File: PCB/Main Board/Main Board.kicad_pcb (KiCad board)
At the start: 2 copper layers, 152.4 x 134.6 mm, 257 parts, among them J101 Conn_Coaxial, J102 Conn_Coaxial, J103 Conn_Coaxial, J104 Conn_Coaxial, J105 Conn_01x01_Pin, J201 USB_C_Receptacle_USB2.0_16P, J801 Conn_01x03_Pin, J802 Screw_Terminal_01x03, K301 AGQ200A12, K401 AGQ200A12, K501 AGQ200A12, K502 AGQ200A12, K503 AGQ200A12, K504 AGQ200A12, K505 AGQ200A12, Q301 TIP41C, Q302 TIP42C, Q401 TIP41C, Q402 TIP42C, Q403 TIP41C, Q404 TIP42C, SW201 SW_Push, SW202 SW_Push, U201 USBLC6-2SC6, U202 STM32F446RETx, U203 ULN2003, U301 DG201, U302 OPA2197xD, U303 OPA2376xxD, U304 OPA2197xD, U401 OPA2197xD, U402 DG201, U403 OPA2197xD, U404 OPA2197xD, U601 INA828D, U602 DG201, U603 OPA2197xD, U604 DG201, U605 OPA2376xxD, U701 INA828D, U702 DG201, U703 OPA2376xxD, U801 LM317_SOT-223, U802 LM317_SOT-223, U803 LM317_SOT-223, U804 LM337_SOT223, Y201 8MHz

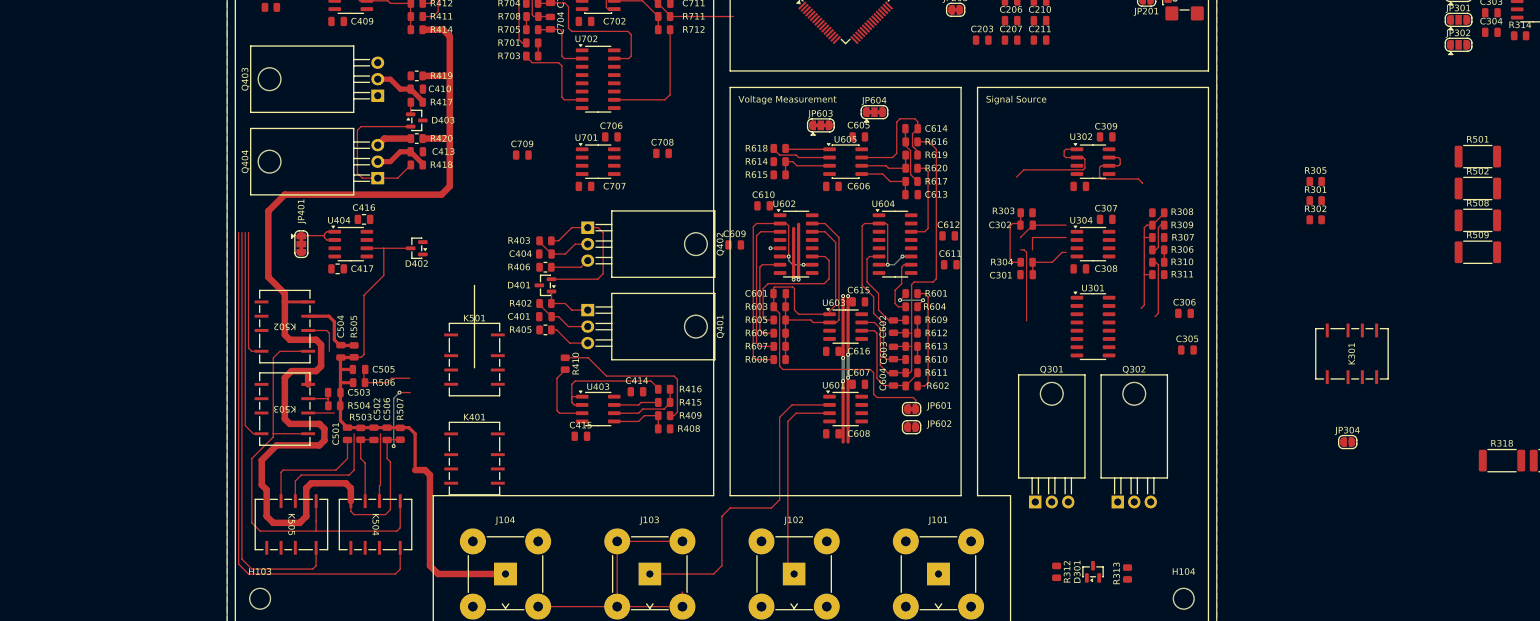
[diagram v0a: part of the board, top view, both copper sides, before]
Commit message: move resistors
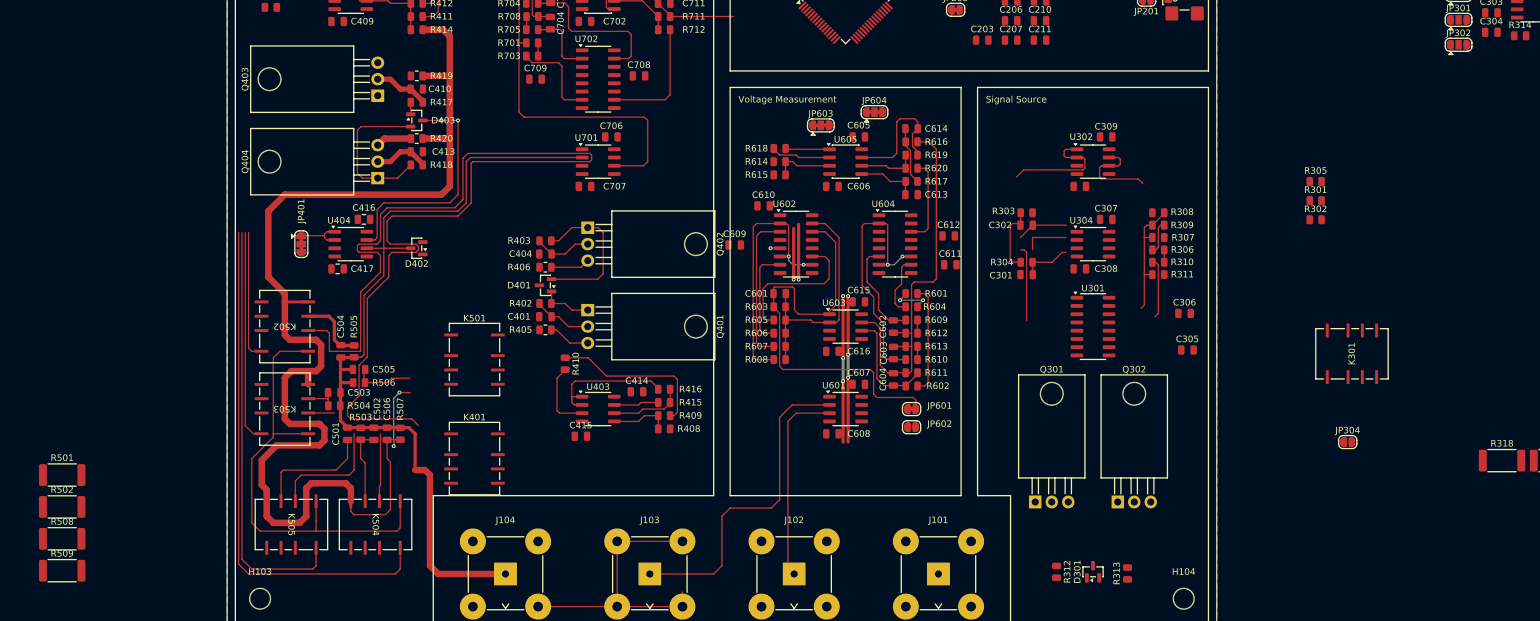
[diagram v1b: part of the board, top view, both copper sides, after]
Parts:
- moved R501 223.5 mm to (19.1, 137.2)
- moved R502 223.5 mm to (19.1, 142.1)
- moved R508 223.5 mm to (19.1, 147.0)
- moved R509 223.5 mm to (19.1, 151.9)
- moved C708 12.5 mm to (107.9, 75.7)
- moved C709 11.9 mm to (91.9, 76.2)
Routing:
- net GUARD: track 350.0 -> 436.5 mm
- net Net-(R701-Pad1): track 11.8 -> 54.9 mm
- net /Auto-Balancing Bridge/In: track 88.7 -> 131.5 mm
- net Net-(D403-K-Pad3): track 0.00 -> 36.3 mm, vias 0 -> 2

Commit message: sig source layout prelim
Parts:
- moved RN301 86.7 mm to (169.7, 96.4)
- moved R319 75.8 mm to (177.8, 130.3), turned to 180 degrees
- moved R314 74.8 mm to (171.7, 90.1), turned to 180 degrees
- moved U303 70.7 mm to (177.4, 83.6)
- moved R316 69.3 mm to (185.7, 130.3), turned to 180 degrees
- moved JP301 69.0 mm to (166.8, 82.3), turned to 180 degrees
- moved JP302 68.8 mm to (166.8, 85.2), turned to 180 degrees
- moved C304 66.4 mm to (175.4, 87.4)
- moved R315 63.0 mm to (185.6, 134.4)
- moved R318 63.0 mm to (177.8, 134.4), turned to 180 degrees
- moved C303 61.3 mm to (179.5, 79.8)
- moved C315 55.4 mm to (187.2, 82.3)
- moved JP304 55.0 mm to (162.3, 137.5)
- moved K301 53.6 mm to (165.4, 130.4), turned to 0 degrees
- moved JP303 51.4 mm to (187.4, 84.7), turned to 180 degrees
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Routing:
- net +1.65VA: track 6.83 -> 64.1 mm, vias 0 -> 4
- net (no net): track 55.9 -> 0.00 mm
- net Net-(JP303-C): track 0.00 -> 31.7 mm
- net Net-(R302-Pad2): track 0.00 -> 25.1 mm
- net Net-(R310-Pad2): track 9.28 -> 27.2 mm
- net Net-(U303B-+): track 0.00 -> 17.7 mm
- net Net-(U304B--): track 19.2 -> 36.7 mm, vias 0 -> 2
- net Net-(JP301-C): track 0.00 -> 16.2 mm
- net Net-(U302A--): track 0.00 -> 15.4 mm
- net Net-(R301-Pad1): track 0.00 -> 14.2 mm, vias 0 -> 2
- net +18V: track 49.2 -> 62.4 mm
- net Net-(JP302-C): track 0.00 -> 13.2 mm, vias 0 -> 2
- net -18V: track 48.6 -> 61.5 mm
- net Net-(C302-Pad2): track 13.1 -> 25.6 mm, vias 0 -> 4
- net Net-(U304A--): track 0.00 -> 12.4 mm
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
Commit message: yipppeee
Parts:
- added REF**: R_0805_2012Metric, Resistor_SMD:R_0805_2012Metric, F.Cu at (69.7, 136.0)
- added REF**: R_0805_2012Metric, Resistor_SMD:R_0805_2012Metric, F.Cu at (71.8, 136.0)
- added REF**: R_0805_2012Metric, Resistor_SMD:R_0805_2012Metric, F.Cu at (69.7, 139.6)
- added REF**: R_0805_2012Metric, Resistor_SMD:R_0805_2012Metric, F.Cu at (71.8, 139.6)
- moved R502 43.2 mm to (62.2, 139.7), turned to 180 degrees
- moved R501 43.2 mm to (62.2, 135.9), turned to 180 degrees
- moved R503 43.1 mm to (23.5, 142.2)
- moved R509 37.6 mm to (54.6, 139.7), turned to 180 degrees
- moved R508 37.2 mm to (54.6, 135.9), turned to 180 degrees
- moved C406 24.2 mm to (71.6, 50.0)
- moved K401 21.3 mm to (76.2, 114.3)
- moved C506 10.7 mm to (77.7, 137.2), turned to 0 degrees
- moved K501 9.92 mm to (76.2, 127.0)
- moved R507 7.89 mm to (77.7, 135.1), turned to 0 degrees
- moved C502 5.25 mm to (67.7, 136.0)
- moved C505 5.21 mm to (68.6, 124.5)
- moved R506 5.21 mm to (68.6, 126.5)
- moved C407 4.33 mm to (54.6, 50.8)
- moved C414 4.10 mm to (103.6, 123.2)
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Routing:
- net /Auto-Balancing Bridge/DC_INT_ISO: track 0.00 -> 203.4 mm, vias 0 -> 2
- net /Auto-Balancing Bridge/R_SEL_100k: track 0.00 -> 187.1 mm
- net GUARD: track 436.5 -> 585.9 mm
- net +12V: track 70.2 -> 190.1 mm, vias 0 -> 8
- net /Auto-Balancing Bridge/R_SEL_1k: track 32.7 -> 102.3 mm
- net /Auto-Balancing Bridge/R_SEL_10: track 65.3 -> 133.3 mm
- net /Auto-Balancing Bridge/R_SEL_10k: track 20.0 -> 87.9 mm
- net /Auto-Balancing Bridge/R_SEL_100: track 80.2 -> 144.1 mm
- net /Auto-Balancing Bridge/In: track 131.5 -> 176.5 mm
- net +1.65VA: track 64.1 -> 33.5 mm, vias 4 -> 0
- net Net-(R404-Pad2): track 25.1 -> 51.7 mm
- net Net-(U403A-+): track 10.9 -> 28.9 mm
- net Net-(JP301-C): track 16.2 -> 0.00 mm
- net Net-(U304A--): track 12.4 -> 0.00 mm
- net Net-(D301-K-Pad3): track 6.82 -> 0.00 mm
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
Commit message: yup
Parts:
- removed REF** (x4): R_0805_2012Metric, Resistor_SMD:R_0805_2012Metric
- removed U203: ULN2003, Package_SO:SOIC-16_3.9x9.9mm_P1.27mm
- added U402: ULN2003, Package_SO:SOIC-16_3.9x9.9mm_P1.27mm, F.Cu at (63.5, 38.1)
- moved C808 39.4 mm to (113.3, 46.4)
- moved C812 39.4 mm to (113.6, 35.0)
- moved R804 39.4 mm to (105.2, 40.7)
- moved R808 39.4 mm to (109.6, 35.0)
- moved U804 39.4 mm to (111.8, 40.6)
- moved C811 33.0 mm to (169.5, 35.0)
- moved R803 33.0 mm to (161.1, 40.7)
- moved C807 33.0 mm to (169.3, 46.3)
- moved D804 33.0 mm to (172.6, 33.9)
- moved FB801 33.0 mm to (169.6, 30.6)
- moved R807 33.0 mm to (165.6, 35.0)
- moved R809 33.0 mm to (169.5, 32.8)
- moved U803 33.0 mm to (167.6, 40.6)
- moved C805 31.8 mm to (131.2, 46.3)
- moved C809 31.8 mm to (131.4, 35.0)
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- renumbered C404 to C402, C405 to C403, C406 to C404, C407 to C405, C408 to C406, C409 to C407, C410 to C408, C413 to C409, C414 to C410, C415 to C411, C416 to C412, C417 to C413, U402 to U403, U403 to U404, U404 to U405
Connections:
- K401 pad 8: /Auto-Balancing Bridge/DC_INT_ISO -> /Auto-Balancing Bridge/DC_ISO
- K501 pad 8: /Auto-Balancing Bridge/R_SEL_100k -> /Auto-Balancing Bridge/SEL_100k
- K502 pad 8: /Auto-Balancing Bridge/R_SEL_10k -> /Auto-Balancing Bridge/SEL_10k
- K503 pad 8: /Auto-Balancing Bridge/R_SEL_1k -> /Auto-Balancing Bridge/SEL_1k
- K504 pad 8: /Auto-Balancing Bridge/R_SEL_100 -> /Auto-Balancing Bridge/SEL_100
- K505 pad 8: /Auto-Balancing Bridge/R_SEL_10 -> /Auto-Balancing Bridge/SEL_10
- U202 pad 29: Net-(U202-PB10) -> /Auto-Balancing Bridge/R_SEL_10k
- U202 pad 33: Net-(U202-PB12) -> /Auto-Balancing Bridge/R_SEL_100
- U202 pad 34: Net-(U202-PB13) -> /Auto-Balancing Bridge/R_SEL_10
- U202 pad 35: Net-(U202-PB14) -> /Auto-Balancing Bridge/DC_INT_ISO
- U202 pad 36: Net-(U202-PB15) -> /Processor/SIG_SOURCE
- U202 pad 61: Net-(U202-PB8) -> /Auto-Balancing Bridge/R_SEL_100k
- U202 pad 62: Net-(U202-PB9) -> /Auto-Balancing Bridge/R_SEL_1k
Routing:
- net /Auto-Balancing Bridge/DC_ISO: track 0.00 -> 205.6 mm, vias 0 -> 2
- net /Auto-Balancing Bridge/DC_INT_ISO: track 203.4 -> 0.00 mm, vias 2 -> 0
- net /Auto-Balancing Bridge/SEL_100k: track 0.00 -> 189.4 mm
- net /Auto-Balancing Bridge/R_SEL_100k: track 187.1 -> 0.00 mm
- net /Auto-Balancing Bridge/SEL_100: track 0.00 -> 146.3 mm
- net /Auto-Balancing Bridge/R_SEL_100: track 144.1 -> 0.00 mm
- net /Auto-Balancing Bridge/SEL_10: track 0.00 -> 135.5 mm
- net /Auto-Balancing Bridge/R_SEL_10: track 133.3 -> 0.00 mm
- net /Auto-Balancing Bridge/SEL_1k: track 0.00 -> 104.5 mm
- net /Auto-Balancing Bridge/R_SEL_1k: track 102.3 -> 0.00 mm
- net /Auto-Balancing Bridge/SEL_10k: track 0.00 -> 90.2 mm
- net /Auto-Balancing Bridge/R_SEL_10k: track 87.9 -> 0.00 mm
- net -18V: track 65.8 -> 130.7 mm, vias 4 -> 6
- net +18V: track 63.9 -> 125.3 mm, vias 4 -> 6
- net Net-(D403-A): track 24.4 -> 18.1 mm
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
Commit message: sig source finished
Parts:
- removed the C311 at (202.1, 147.2)
- removed the C312 at (202.0, 143.9)
- removed the C313 at (210.5, 142.4)
- removed the C314 at (210.3, 148.0)
- removed the C408 at (73.7, 77.7)
- removed the C409 at (73.7, 87.4)
- removed the R312 at (191.7, 138.7)
- removed the R317 at (181.8, 127.2)
- removed the R405 at (91.4, 114.8)
- removed the R406 at (91.4, 105.2)
- removed R419, R420: 100m, Resistor_SMD:R_0805_2012Metric
- added C301: 10µ, Capacitor_SMD:C_0805_2012Metric, F.Cu at (184.5, 129.8)
- added C303: 1u, Capacitor_SMD:C_0805_2012Metric, F.Cu at (179.5, 124.3)
- added C305: 10µ, Capacitor_SMD:C_0805_2012Metric, F.Cu at (170.0, 129.8)
- added C403: 1u, Capacitor_SMD:C_0805_2012Metric, F.Cu at (38.7, 103.3)
- added C404: 1u, Capacitor_SMD:C_0805_2012Metric, F.Cu at (38.7, 106.3)
- added C405: 10µ, Capacitor_SMD:C_0805_2012Metric, F.Cu at (38.7, 109.3)
- added C406: 10µ, Capacitor_SMD:C_0805_2012Metric, F.Cu at (38.7, 112.3)
- added Q303: 2N7002, Package_TO_SOT_SMD:SOT-23, F.Cu at (183.9, 156.8)
- added R309: 2k, Resistor_SMD:R_0805_2012Metric, F.Cu at (173.8, 129.8)
- added R314: 100, Resistor_SMD:R_0805_2012Metric, F.Cu at (171.9, 145.7)
- added R315: 100, Resistor_SMD:R_0805_2012Metric, F.Cu at (169.8, 142.2)
- added R316: 100, Resistor_SMD:R_0805_2012Metric, F.Cu at (169.8, 145.7)
- added R320: 2k, Resistor_SMD:R_0805_2012Metric, F.Cu at (180.9, 129.8)
- Q301, Q302, Q401, Q404: moved to B.Cu
- Q402: renamed from Q403; moved to B.Cu
- Q403: renamed from Q402; moved to B.Cu
- R313: value 2k -> 100
- moved J101 208.2 mm to (166.5, 157.1), turned to -90 degrees
- moved C306 79.5 mm to (163.6, 158.2), turned to -90 degrees
- moved C401 55.0 mm to (38.7, 97.2)
- moved C402 52.8 mm to (38.7, 100.2)
- moved Q401 46.4 mm to (67.4, 78.8), turned to 90 degrees
- moved Q402 46.1 mm to (99.8, 111.8), turned to -90 degrees
- moved Q403 33.5 mm to (67.4, 91.5), turned to 90 degrees
- moved Q404 33.0 mm to (99.8, 99.1), turned to -90 degrees
- moved K301 26.6 mm to (176.2, 154.7), turned to -90 degrees
- moved D301 21.1 mm to (177.3, 128.8), turned to 90 degrees
- moved R313 20.9 mm to (171.9, 142.2), turned to -90 degrees
- moved R307 17.3 mm to (175.0, 144.0), turned to -90 degrees
- moved JP301 15.6 mm to (169.2, 151.4), turned to 90 degrees
- moved R308 14.7 mm to (183.2, 144.0), turned to -90 degrees
- moved R305 13.5 mm to (187.3, 144.0), turned to -90 degrees
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- renumbered C209 to C201, C204 to C202, C201 to C203, C202 to C204, C203 to C205, C205 to C206, C206 to C207, C207 to C208, C208 to C209, C301 to C304, C315 to C306, C303 to C307, C305 to C308, C307 to C309, C309 to C310, C304 to C311, C306 to C312, C308 to C313, C310 to C314, C403 to C407, C404 to C408, C406 to C409, C412 to C411, C405 to C412, C407 to C413, C411 to C414, C413 to C415, C602 to C601, C614 to C602, C613 to C604, C604 to C605, C605 to C606, C609 to C608, C611 to C609, C615 to C610, C606 to C611, C608 to C612, C610 to C613, C612 to C614, C616 to C615, C601 to C616, C703 to C701, C711 to C702, C704 to C703, C710 to C704, C701 to C706, C706 to C707, C702 to C709, C707 to C710, C709 to C711, C805 to C801, C809 to C802, C806 to C803, C810 to C804, C801 to C805, C803 to C806, C802 to C807, C804 to C808, C807 to C809, C811 to C810, C808 to C811, D403 to D402, D402 to D403, D803 to D801, D801 to D802, D802 to D803, J105 to J101, J101 to J102, J102 to J103, J103 to J104, J104 to J105, J802 to J801, J801 to J802, JP203 to JP202, JP202 to JP203, JP304 to JP301, JP303 to JP302, JP301 to JP303, JP302 to JP304, JP603 to JP601, JP604 to JP602, JP601 to JP603, JP602 to JP604, K505 to K501, K504 to K502, K502 to K504, K501 to K505, R205 to R204, R206 to R205, R207 to R206, R208 to R207, R204 to R208, R307 to R301, R311 to R302, R308 to R303, R315 to R304, R318 to R305, R309 to R306, R316 to R307, R319 to R308, R306 to R310, R310 to R311, R304 to R312, R303 to R317, R305 to R318, R301 to R319, R302 to R321, R314 to R322, R404 to R401, R408 to R402, R415 to R403, R409 to R404, R416 to R405, R402 to R406, R417 to R407, R410 to R408, R401 to R409, R403 to R410, R418 to R412, R407 to R413, R412 to R414, R413 to R415, R414 to R416, R508 to R502, R502 to R503, R509 to R504, R503 to R505, R504 to R506, R505 to R507, R506 to R508, R507 to R509, R609 to R601, R612 to R602, R601 to R603, R610 to R605, R613 to R606, R616 to R607, R617 to R608, R619 to R609, R602 to R610, R620 to R612, R618 to R613, R608 to R616, R603 to R617, R605 to R618, R606 to R619, R607 to R620, R704 to R701, R707 to R702, R701 to R703, R703 to R704, R708 to R706, R709 to R707, R710 to R708, R711 to R709, R702 to R710, R706 to R711, R805 to R801, R801 to R802, R806 to R803, R802 to R804, R807 to R805, R809 to R806, R803 to R807, R804 to R808, R808 to R809, SW202 to SW201, SW201 to SW202, U302 to U301, U301 to U302, U304 to U303, U303 to U304, U404 to U401, U401 to U402, U405 to U403, U403 to U404, U402 to U405, U604 to U601, U601 to U602, U605 to U603, U603 to U604, U602 to U605, U702 to U701, U701 to U702
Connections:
- C402 pad 2: -18V -> +18V
- D301 pad 3: Net-(D301-K-Pad3) -> Net-(C303-Pad2)
- D401 pad 3: Net-(D401-K-Pad3) -> Net-(C403-Pad2)
- D402 pad 3: Net-(D403-K-Pad3) -> Net-(C404-Pad2)
- K301 pad 8: /Processor/SIG_SOURCE -> /Signal Source/RELAY_DRIVE
- Q402 pad 3: Net-(Q403-E) -> /Auto-Balancing Bridge/OUT+
- Q403 pad 3: Net-(Q402-E) -> Net-(Q401-E)
- Q404 pad 3: Net-(Q404-E) -> /Auto-Balancing Bridge/OUT+
- R313 pad 1: Net-(D301-A) -> Net-(Q301-E)
- R313 pad 2: -18V -> Net-(R313-Pad2)
- R401 pad 2: Net-(R404-Pad2) -> Net-(Q401-E)
- R404 pad 2: Net-(R404-Pad2) -> Net-(Q401-E)
- R408 pad 1: Net-(R404-Pad2) -> Net-(Q401-E)
- U303 pad 7: Net-(D301-K-Pad3) -> Net-(C303-Pad1)
- U402 pad 1: Net-(D401-K-Pad3) -> Net-(C403-Pad1)
- U403 pad 7: Net-(D403-K-Pad3) -> Net-(C404-Pad1)
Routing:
- net /Signal Source/AUX_DAC_OUT: track 7.94 -> 112.0 mm
- net /Processor/SIG_SOURCE: track 0.00 -> 82.0 mm
- net Net-(Q401-E): track 8.48 -> 66.0 mm
- net Net-(R404-Pad2): track 51.7 -> 0.00 mm
- net Net-(D403-K-Pad3): track 34.7 -> 0.00 mm, vias 2 -> 0
- net (no net): track 0.00 -> 34.7 mm, vias 0 -> 2
- net +1.65VA: track 33.5 -> 58.4 mm, vias 0 -> 4
- net /Signal Source/Out: track 0.00 -> 22.6 mm
- net /Auto-Balancing Bridge/OUT+: track 211.5 -> 225.2 mm
- net Net-(Q301-E): track 5.67 -> 19.3 mm
- net Net-(K301-Pad2): track 0.00 -> 12.9 mm
- net Net-(R307-Pad2): track 0.00 -> 10.6 mm
- net Net-(R304-Pad2): track 0.00 -> 10.6 mm
- net Net-(U303B--): track 36.7 -> 26.5 mm
- net Net-(D301-A): track 0.00 -> 10.1 mm
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
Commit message: minor
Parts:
- J101: footprint Connector_PinHeader_2.54mm:PinHeader_1x01_P2.54mm_Vertical -> Connector_PinHeader_2.54mm:PinHeader_1x01_P2.54mm_Horizontal
- moved C306 1.91 mm to (165.6, 158.1)
- moved J101 1.91 mm to (168.4, 157.1)
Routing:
- net Net-(Q301-E): track 19.3 -> 41.8 mm, vias 0 -> 2
- net Net-(Q301-B): track 3.44 -> 19.3 mm
- net Net-(U303B--): track 26.5 -> 38.3 mm
- net +18V: track 125.3 -> 137.2 mm
- net -18V: track 133.7 -> 144.6 mm
- net Net-(U303A--): track 2.41 -> 13.0 mm
- net +1.65VA: track 58.4 -> 65.7 mm
- net Net-(D301-A): track 10.1 -> 12.5 mm
- net /Signal Source/AUX_DAC_OUT: track 112.0 -> 110.0 mm
- net Net-(JP302-C): track 31.7 -> 32.6 mm

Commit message: hello
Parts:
- added R501: 100, Resistor_SMD:R_0805_2012Metric, F.Cu at (71.9, 135.9)
- added R511: 100, Resistor_SMD:R_0805_2012Metric, F.Cu at (71.9, 139.4)
- added R512: 100, Resistor_SMD:R_0805_2012Metric, F.Cu at (69.8, 139.4)
- J105: renamed from J101; footprint Connector_PinHeader_2.54mm:PinHeader_1x01_P2.54mm_Horizontal -> Connector_PinHeader_2.54mm:PinHeader_1x01_P2.54mm_Vertical
- JP701, JP702: footprint Jumper:SolderJumper-3_P1.3mm_Bridged123_RoundedPad1.0x1.5mm -> Jumper:SolderJumper-3_P1.3mm_Bridged12_RoundedPad1.0x1.5mm
- Q302: renamed from Q301; footprint Package_TO_SOT_THT:TO-220-3_Horizontal_TabDown -> Package_TO_SOT_THT:TO-220-3_Horizontal_TabUp
- Q303: renamed from Q302; footprint Package_TO_SOT_THT:TO-220-3_Horizontal_TabDown -> Package_TO_SOT_THT:TO-220-3_Horizontal_TabUp
- Q401, Q404: footprint Package_TO_SOT_THT:TO-220-3_Horizontal_TabDown -> Package_TO_SOT_THT:TO-220-3_Horizontal_TabUp
- Q402: renamed from Q403; footprint Package_TO_SOT_THT:TO-220-3_Horizontal_TabDown -> Package_TO_SOT_THT:TO-220-3_Horizontal_TabUp
- Q403: renamed from Q402; footprint Package_TO_SOT_THT:TO-220-3_Horizontal_TabDown -> Package_TO_SOT_THT:TO-220-3_Horizontal_TabUp
- moved Y201 48.2 mm to (124.2, 69.3)
- moved R502 46.8 mm to (69.8, 135.9)
- moved Q403 45.4 mm to (68.6, 78.7), turned to 90 degrees
- moved Q401 44.0 mm to (96.5, 111.8), turned to -90 degrees
- moved JP702 38.8 mm to (99.6, 69.6)
- moved JP701 37.2 mm to (103.6, 57.4), turned to 180 degrees
- moved Q404 32.1 mm to (68.6, 91.5), turned to 90 degrees
- moved Q402 30.1 mm to (96.5, 99.1), turned to -90 degrees
- moved Q303 4.93 mm to (168.7, 136.9), turned to 0 degrees
- moved R404 4.15 mm to (53.3, 64.5), turned to 180 degrees
- moved R401 3.42 mm to (53.3, 62.5)
- moved C502 0.13 mm to (67.7, 135.9)
- turned Q302 to 0 degrees
- renumbered C203 to C201, C204 to C202, C205 to C203, C202 to C204, C206 to C205, C207 to C206, C208 to C207, C209 to C208, C201 to C209, C304 to C301, C307 to C303, C311 to C304, C308 to C305, C312 to C306, C309 to C307, C313 to C308, C310 to C309, C314 to C310, C303 to C311, C301 to C312, C305 to C313, C306 to C314, C403 to C401, C401 to C402, C405 to C403, C407 to C404, C408 to C405, C412 to C406, C409 to C407, C413 to C408, C404 to C409, C402 to C410, C406 to C411, C410 to C412, C414 to C413, C411 to C414, C616 to C601, C601 to C602, C605 to C604, C606 to C605, C611 to C606, C612 to C608, C608 to C609, C613 to C610, C609 to C611, C614 to C612, C604 to C613, C602 to C614, C610 to C615, C615 to C616, C706 to C701, C709 to C702, C701 to C703, C703 to C704, C707 to C706, C710 to C707, C711 to C709, C704 to C710, C702 to C711, C805 to C801, C807 to C802, C806 to C803, C808 to C804, C801 to C805, C803 to C806, C809 to C807, C811 to C808, C802 to C809, C804 to C810, C810 to C811, D403 to D402, D402 to D403, D802 to D801, D803 to D802, D801 to D803, J102 to J101, J103 to J102, J104 to J103, J105 to J104, J802 to J801, J801 to J802, JP203 to JP202, JP202 to JP203, JP303 to JP301, JP304 to JP302, JP302 to JP303, JP301 to JP304, JP603 to JP601, JP604 to JP602, JP601 to JP603, JP602 to JP604, K505 to K501, K504 to K502, K502 to K504, K501 to K505, Q303 to Q301, R208 to R204, R204 to R205, R205 to R206, R206 to R207, R207 to R208, R319 to R301, R321 to R302, R317 to R303, R312 to R304, R318 to R305, R310 to R306, R301 to R307, R303 to R308, R306 to R309, R311 to R310, R309 to R311, R320 to R312, R302 to R313, R322 to R314, R304 to R315, R307 to R316, R313 to R317, R315 to R318, R305 to R319, R308 to R320, R314 to R321, R316 to R322, R409 to R401, R406 to R402, R410 to R403, R401 to R404, R413 to R405, R402 to R406, R404 to R407, R411 to R409, R414 to R410, R415 to R411, R416 to R412, R403 to R413, R405 to R414, R407 to R415, R412 to R416, R505 to R502, R501 to R503, R503 to R504, R506 to R505, R507 to R506, R508 to R507, R509 to R508, R502 to R509, R504 to R510, R603 to R601, R610 to R602, R617 to R603, R618 to R605, R619 to R606, R620 to R607, R616 to R608, R601 to R609, R605 to R610, R602 to R612, R606 to R613, R607 to R616, R608 to R617, R613 to R618, R609 to R619, R612 to R620, R703 to R701, R710 to R702, R704 to R703, R701 to R704, R711 to R706, R702 to R707, R706 to R708, R707 to R709, R708 to R710, R709 to R711, R802 to R801, R804 to R802, R807 to R803, R808 to R804, R801 to R805, R803 to R806, R805 to R807, R809 to R808, R806 to R809, SW202 to SW201, SW201 to SW202, U302 to U301, U301 to U302, U304 to U303, U303 to U304, U402 to U401, U405 to U402, U404 to U403, U401 to U404, U403 to U405, U602 to U601, U605 to U602, U604 to U603, U601 to U604, U603 to U605, U702 to U701, U701 to U702
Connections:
- R502 pad 2: Net-(C502-Pad2) -> Net-(R502-Pad2)
- U202 pad 10: /Processor/VAmp.x3 -> unconnected-(U202-PC2-Pad10)
- U202 pad 11: /Processor/VAmp.~{x100} -> unconnected-(U202-PC3-Pad11)
- U202 pad 14: /Processor/VAmp.Out -> unconnected-(U202-PA0-Pad14)
- U202 pad 15: /Current Amplifier/Out -> unconnected-(U202-PA1-Pad15)
- U202 pad 16: /Processor/SW1 -> unconnected-(U202-PA2-Pad16)
- U202 pad 17: unconnected-(U202-PA3-Pad17) -> /Processor/VAmp.Out
- U202 pad 2: /Processor/IAmp.AC_100 -> unconnected-(U202-PC13-Pad2)
- U202 pad 24: /Processor/VAmp.AC_EN -> unconnected-(U202-PC4-Pad24)
- U202 pad 25: /Processor/VAmp.AC_100 -> unconnected-(U202-PC5-Pad25)
- U202 pad 29: /Auto-Balancing Bridge/R_SEL_10k -> unconnected-(U202-PB10-Pad29)
- U202 pad 3: /Processor/IAmp.AC_1k -> unconnected-(U202-PC14-Pad3)
- U202 pad 33: /Auto-Balancing Bridge/R_SEL_100 -> unconnected-(U202-PB12-Pad33)
- U202 pad 34: /Auto-Balancing Bridge/R_SEL_10 -> unconnected-(U202-PB13-Pad34)
- U202 pad 35: /Auto-Balancing Bridge/DC_INT_ISO -> unconnected-(U202-PB14-Pad35)
- U202 pad 36: /Processor/SIG_SOURCE -> unconnected-(U202-PB15-Pad36)
- U202 pad 37: /Processor/VAmp.AC_1k -> unconnected-(U202-PC6-Pad37)
- U202 pad 38: /Processor/VAmp.AC_10k -> unconnected-(U202-PC7-Pad38)
- U202 pad 39: /Current Amplifier//4 -> unconnected-(U202-PC8-Pad39)
- U202 pad 4: /Processor/IAmp.AC_10k -> unconnected-(U202-PC15-Pad4)
- U202 pad 40: /Current Amplifier/x1 -> unconnected-(U202-PC9-Pad40)
- U202 pad 51: /Current Amplifier/x3 -> unconnected-(U202-PC10-Pad51)
- U202 pad 52: /Current Amplifier/~{x100} -> unconnected-(U202-PC11-Pad52)
- U202 pad 53: /Processor/IAmp.AC_EN -> unconnected-(U202-PC12-Pad53)
- U202 pad 56: /Processor/Source.~{x4} -> /Auto-Balancing Bridge/DC_INT_ISO
- U202 pad 57: /Processor/Source./10 -> /Auto-Balancing Bridge/R_SEL_100k
- U202 pad 58: unconnected-(U202-PB6-Pad58) -> /Auto-Balancing Bridge/R_SEL_10k
- U202 pad 59: unconnected-(U202-PB7-Pad59) -> /Auto-Balancing Bridge/R_SEL_1k
- U202 pad 61: /Auto-Balancing Bridge/R_SEL_100k -> /Auto-Balancing Bridge/R_SEL_100
- U202 pad 62: /Auto-Balancing Bridge/R_SEL_1k -> /Auto-Balancing Bridge/R_SEL_10
- U202 pad 8: /Processor/VAmp./4 -> unconnected-(U202-PC0-Pad8)
- U202 pad 9: /Processor/VAmp.x1 -> /Current Amplifier/Out
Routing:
- net /Auto-Balancing Bridge/DC_INT_ISO: track 0.00 -> 85.4 mm
- net /Auto-Balancing Bridge/R_SEL_100k: track 0.00 -> 84.5 mm
- net /Auto-Balancing Bridge/R_SEL_10k: track 0.00 -> 83.8 mm
- net /Auto-Balancing Bridge/R_SEL_1k: track 0.00 -> 83.1 mm
- net /Auto-Balancing Bridge/R_SEL_100: track 0.00 -> 82.1 mm
- net /Auto-Balancing Bridge/R_SEL_10: track 0.00 -> 81.1 mm
- net -18V: track 144.6 -> 203.9 mm, vias 6 -> 10
- net +18V: track 137.2 -> 189.4 mm, vias 6 -> 10
- net Net-(Q302-E): track 41.8 -> 0.00 mm, vias 2 -> 0
- net Net-(D301-A): track 12.5 -> 54.3 mm, vias 0 -> 2
- net /Current Amplifier/Out: track 20.0 -> 42.1 mm
- net unconnected-(U202-PC0-Pad8): track 0.00 -> 19.3 mm
- net /Processor/VAmp.Out: track 19.9 -> 36.8 mm
- net Net-(Q401-E): track 66.0 -> 51.7 mm
- net /Auto-Balancing Bridge/OUT+: track 225.2 -> 211.4 mm, vias 4 -> 5
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
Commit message: :(
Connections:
- U202 pad 49: unconnected-(U202-PA14-Pad49) -> /Auto-Balancing Bridge/DC_INT_ISO
- U202 pad 50: unconnected-(U202-PA15-Pad50) -> /Auto-Balancing Bridge/R_SEL_100k
- U202 pad 51: unconnected-(U202-PC10-Pad51) -> /Auto-Balancing Bridge/R_SEL_10k
- U202 pad 52: unconnected-(U202-PC11-Pad52) -> /Auto-Balancing Bridge/R_SEL_1k
- U202 pad 53: unconnected-(U202-PC12-Pad53) -> /Auto-Balancing Bridge/R_SEL_100
- U202 pad 54: unconnected-(U202-PD2-Pad54) -> /Auto-Balancing Bridge/R_SEL_10
- U202 pad 55: unconnected-(U202-PB3-Pad55) -> /Auto-Balancing Bridge/AC_EN
- U202 pad 56: /Auto-Balancing Bridge/DC_INT_ISO -> /Auto-Balancing Bridge/AC_10k
- U202 pad 57: /Auto-Balancing Bridge/R_SEL_100k -> /Auto-Balancing Bridge/AC_100
- U202 pad 58: /Auto-Balancing Bridge/R_SEL_10k -> /Auto-Balancing Bridge/AC_1k
- U202 pad 59: /Auto-Balancing Bridge/R_SEL_1k -> unconnected-(U202-PB7-Pad59)
- U202 pad 61: /Auto-Balancing Bridge/R_SEL_100 -> unconnected-(U202-PB8-Pad61)
- U202 pad 62: /Auto-Balancing Bridge/R_SEL_10 -> unconnected-(U202-PB9-Pad62)
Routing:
- net +18V: track 189.4 -> 282.0 mm, vias 10 -> 14
- net /Auto-Balancing Bridge/AC_EN: track 0.00 -> 85.1 mm, vias 0 -> 2
- net /Auto-Balancing Bridge/AC_100: track 0.00 -> 79.4 mm, vias 0 -> 2
- net /Auto-Balancing Bridge/AC_10k: track 0.00 -> 79.0 mm
- net -18V: track 203.9 -> 278.4 mm, vias 10 -> 12
- net /Auto-Balancing Bridge/AC_1k: track 0.00 -> 71.7 mm, vias 0 -> 2
- net +12V: track 190.1 -> 239.1 mm, vias 8 -> 10
- net /Auto-Balancing Bridge/DC_INT_ISO: track 85.4 -> 84.5 mm
- net /Auto-Balancing Bridge/R_SEL_100k: track 84.5 -> 83.8 mm
- net /Auto-Balancing Bridge/R_SEL_1k: track 83.1 -> 82.4 mm
- net /Auto-Balancing Bridge/R_SEL_10k: track 83.8 -> 83.1 mm
- net /Auto-Balancing Bridge/R_SEL_100: track 82.1 -> 81.6 mm
- net /Auto-Balancing Bridge/R_SEL_10: track 81.1 -> 80.6 mm
